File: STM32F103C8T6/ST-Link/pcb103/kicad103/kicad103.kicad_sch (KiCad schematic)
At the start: 31 parts, among them IC1 LD1117DT33TR, J1 0480372200, J2 Conn_01x02_Socket, J3 Conn_02x05_Odd_Even, J5 Conn_01x16_Pin, J7 Conn_01x04_Pin, J8 Conn_01x05_Socket, J9 Conn_01x17_Pin, U1 STM32F103C8T6, Y1 8MHz 20pF

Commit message: Generate BOM
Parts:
- C1: JLC # (none) -> C24497
- C2: JLC # (none) -> C15850
- C3, C4, C5, C6, C7: JLC # (none) -> C14663
- C8, C9: JLC # (none) -> C1557
- D1: JLC # (none) -> C8598
- D2: JLC # (none) -> C84256
- D3: JLC # (none) -> C2296
- IC1: JLC # (none) -> C132629
- J3: JLC # (none) -> C2881910
- R1, R2, R4, R5: JLC # (none) -> C4310
- R3: JLC # (none) -> C25118
- R6: JLC # (none) -> C2078575
- U1: JLC # (none) -> C8734
- Y1: JLC # (none) -> C115962
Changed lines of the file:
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@@
+      (effects (font (size 1.27 1.27)) hide)
+    )
+    (property "JLC #" "C25118" (at 45.085 100.33 0)
       (effects (font (size 1.27 1.27)) hide)
     )
@@
     )
     (property "Datasheet" "~" (at 198.12 146.685 0)
+      (effects (font (size 1.27 1.27)) hide)
+    )
+    (property "JLC #" "" (at 198.12 146.685 0)
       (effects (font (size 1.27 1.27)) hide)
     )
@@
       (effects (font (size 1.27 1.27)) hide)
     )
+    (property "JLC #" "C1557" (at 50.165 88.265 0)
+      (effects (font (size 1.27 1.27)) hide)
+    )
     (pin "1")
     (pin "2")
@@
       (effects (font (size 1.27 1.27)) (justify left top) hide)
     )
+    (property "JLC #" "C132629" (at 208.915 34.925 0)
+      (effects (font (size 1.27 1.27)) hide)
+    )
     (pin "1")
     (pin "3")
@@
       (effects (font (size 1.27 1.27)) hide)
     )
+    (property "JLC #" "C14663" (at 55.88 62.865 0)
+      (effects (font (size 1.27 1.27)) hide)
+    )
     (pin "1")
     (pin "2")
@@
     )
     (property "Datasheet" "~" (at 241.3 146.685 0)
+      (effects (font (size 1.27 1.27)) hide)
+    )
+    (property "JLC #" "" (at 241.3 146.685 0)
       (effects (font (size 1.27 1.27)) hide)
     )
@@
     )
     (property "Datasheet" "~" (at 95.25 62.865 0)
+      (effects (font (size 1.27 1.27)) hide)
+    )
+    (property "JLC #" "C14663" (at 95.25 62.865 0)
       (effects (font (size 1.27 1.27)) hide)
     )
@@
       (effects (font (size 1.27 1.27)) hide)
     )
+    (property "JLC #" "C1557" (at 37.465 105.41 0)
+      (effects (font (size 1.27 1.27)) hide)
+    )
     (pin "1")
     (pin "2")
@@
       (effects (font (size 1.27 1.27)) hide)
     )
+    (property "JLC #" "" (at 163.83 38.735 0)
+      (effects (font (size 1.27 1.27)) hide)
+    )
     (pin "1")
     (pin "2")
@@
     )
     (property "Datasheet" "~" (at 15.24 29.845 0)
+      (effects (font (size 1.27 1.27)) hide)
+    )
+    (property "JLC #" "" (at 15.24 29.845 0)
       (effects (font (size 1.27 1.27)) hide)
     )
@@
     )
     (property "Datasheet" "~" (at 199.39 104.14 0)
+      (effects (font (size 1.27 1.27)) hide)
+    )
+    (property "JLC #" "" (at 199.39 104.14 0)
       (effects (font (size 1.27 1.27)) hide)
     )
@@
       (effects (font (size 1.27 1.27)) hide)
     )
+    (property "JLC #" "C4310" (at 274.32 42.545 0)
+      (effects (font (size 1.27 1.27)) hide)
+    )
     (pin "1")
     (pin "2")
@@
       (effects (font (size 1.27 1.27)) hide)
     )
+    (property "JLC #" "C14663" (at 69.215 62.865 0)
+      (effects (font (size 1.27 1.27)) hide)
+    )
     (pin "1")
     (pin "2")
@@
     )
     (property "Datasheet" "~" (at 15.24 22.86 0)
+      (effects (font (size 1.27 1.27)) hide)
+    )
+    (property "JLC #" "" (at 15.24 22.86 0)
       (effects (font (size 1.27 1.27)) hide)
     )
@@
     )
     (property "Datasheet" "~" (at 39.37 173.355 0)
+      (effects (font (size 1.27 1.27)) hide)
+    )
+    (property "JLC #" "C2881910" (at 39.37 173.355 0)
       (effects (font (size 1.27 1.27)) hide)
     )
@@
       (effects (font (size 1.27 1.27)) hide)
     )
+    (property "JLC #" "C15850" (at 252.095 41.275 0)
+      (effects (font (size 1.27 1.27)) hide)
+    )
     (pin "1")
     (pin "2")
@@
       (effects (font (size 1.27 1.27)) hide)
     )
+    (property "JLC #" "C24497" (at 196.85 35.56 0)
+      (effects (font (size 1.27 1.27)) hide)
+    )
     (pin "1")
     (pin "2")
@@
     )
     (property "Datasheet" "~" (at 131.445 110.49 0)
+      (effects (font (size 1.27 1.27)) hide)
+    )
+    (property "JLC #" "C4310" (at 131.445 110.49 0)
       (effects (font (size 1.27 1.27)) hide)
     )
@@
       (effects (font (size 1.27 1.27)) hide)
     )
+    (property "JLC #" "C2296" (at 52.07 107.95 0)
+      (effects (font (size 1.27 1.27)) hide)
+    )
     (pin "1")
     (pin "2")
@@
     )
     (property "Datasheet" "~" (at 266.065 34.925 0)
+      (effects (font (size 1.27 1.27)) hide)
+    )
+    (property "JLC #" "C84256" (at 266.065 34.925 0)
       (effects (font (size 1.27 1.27)) hide)
     )
@@
       (effects (font (size 1.27 1.27)) hide)
     )
+    (property "JLC #" "C115962" (at 37.465 89.535 0)
+      (effects (font (size 1.27 1.27)) hide)
+    )
     (pin "1")
     (pin "2")
@@
     )
     (property "Datasheet" "https://www.st.com/resource/en/datasheet/stm32f103c8.pdf" (at 84.455 125.73 0)
+      (effects (font (size 1.27 1.27)) hide)
+    )
+    (property "JLC #" "C8734" (at 84.455 125.73 0)
       (effects (font (size 1.27 1.27)) hide)
     )
@@
       (effects (font (size 1.27 1.27)) hide)
     )
+    (property "JLC #" "" (at 15.24 15.875 0)
+      (effects (font (size 1.27 1.27)) hide)
+    )
     (pin "1")
     (instances
@@
     (property "Arrow Price/Stock" "https://www.arrow.com/en/products/0480372200/molex?region=nac" (at 129.54 -958.725 0)
       (effects (font (size 1.27 1.27)) (justify left top) hide)
+    )
+    (property "JLC #" "" (at 113.03 36.195 0)
+      (effects (font (size 1.27 1.27)) hide)
     )
     (pin "1")
@@
       (effects (font (size 1.27 1.27)) hide)
     )
+    (property "JLC #" "C4310" (at 50.165 133.35 0)
+      (effects (font (size 1.27 1.27)) hide)
+    )
     (pin "1")
     (pin "2")
@@
       (effects (font (size 1.27 1.27)) hide)
     )
+    (property "JLC #" "C4310" (at 43.18 115.57 0)
+      (effects (font (size 1.27 1.27)) hide)
+    )
     (pin "1")
     (pin "2")
@@
     )
     (property "Datasheet" "~" (at 238.76 104.14 0)
+      (effects (font (size 1.27 1.27)) hide)
+    )
+    (property "JLC #" "" (at 238.76 104.14 0)
       (effects (font (size 1.27 1.27)) hide)
     )
@@
       (effects (font (size 1.27 1.27)) hide)
     )
+    (property "JLC #" "C8598" (at 186.69 28.575 0)
+      (effects (font (size 1.27 1.27)) hide)
+    )
     (pin "1")
     (pin "2")
@@
       (effects (font (size 1.27 1.27)) hide)
     )
+    (property "JLC #" "C14663" (at 82.55 62.865 0)
+      (effects (font (size 1.27 1.27)) hide)
+    )
     (pin "1")
     (pin "2")
@@
       (effects (font (size 1.27 1.27)) hide)
     )
+    (property "JLC #" "C2078575" (at 137.16 150.495 0)
+      (effects (font (size 1.27 1.27)) hide)
+    )
     (pin "1")
     (pin "2")
@@
       (effects (font (size 1.27 1.27)) hide)
     )
+    (property "JLC #" "C14663" (at 107.95 62.865 0)
+      (effects (font (size 1.27 1.27)) hide)
+    )

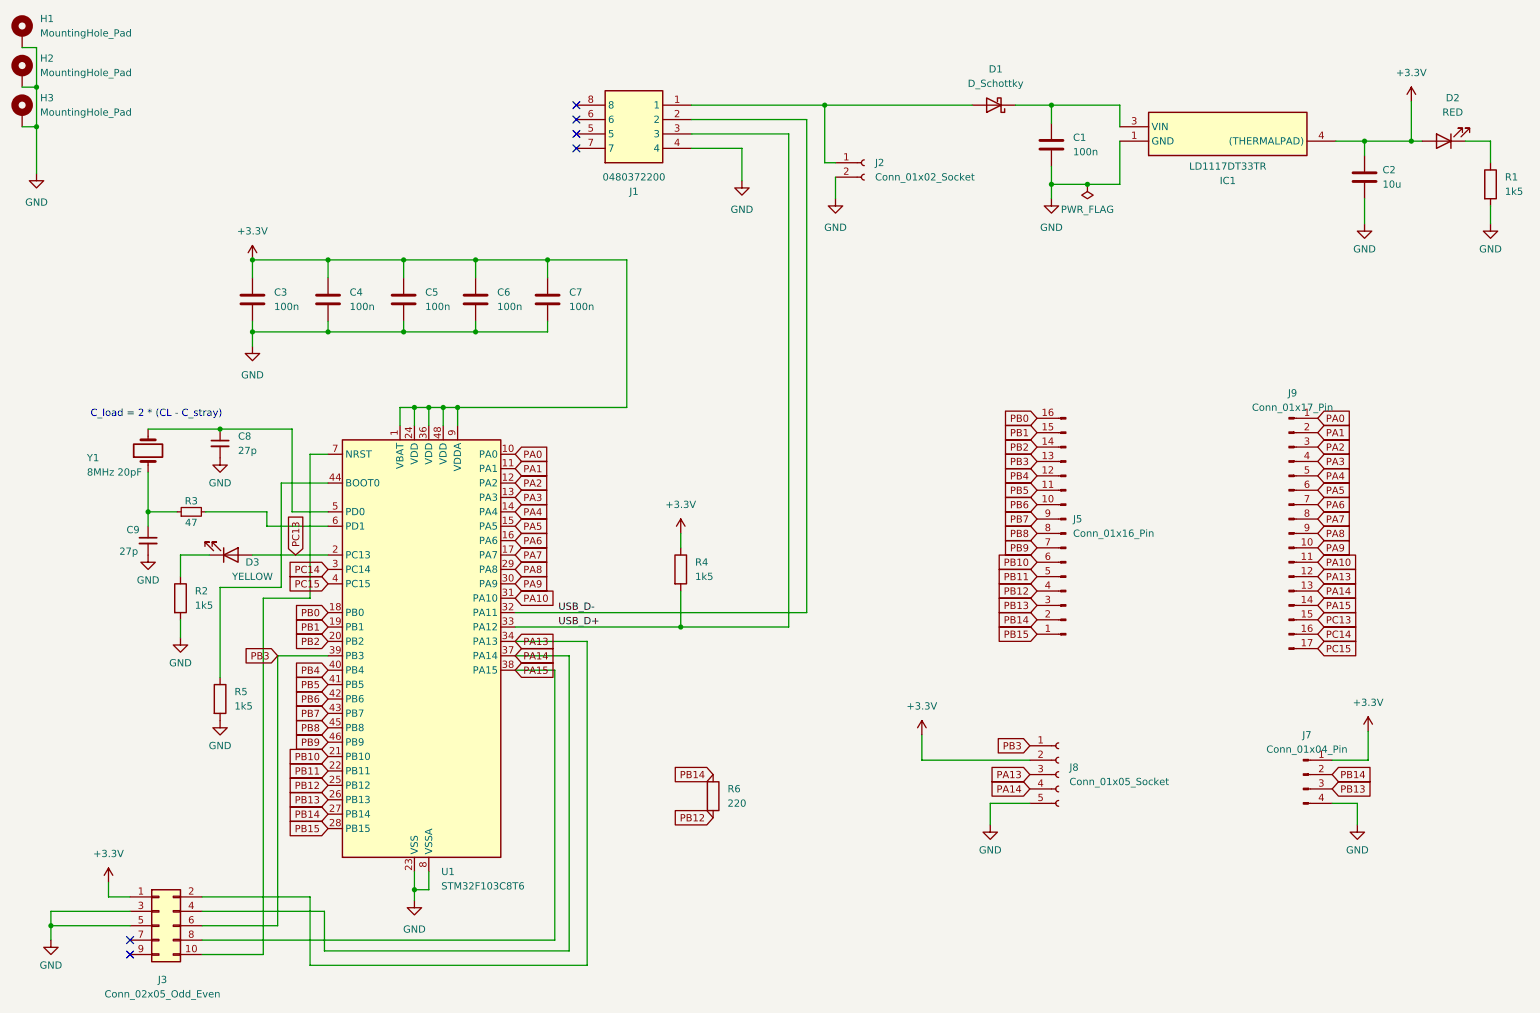
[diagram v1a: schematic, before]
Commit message: Replace 3.3V regulator
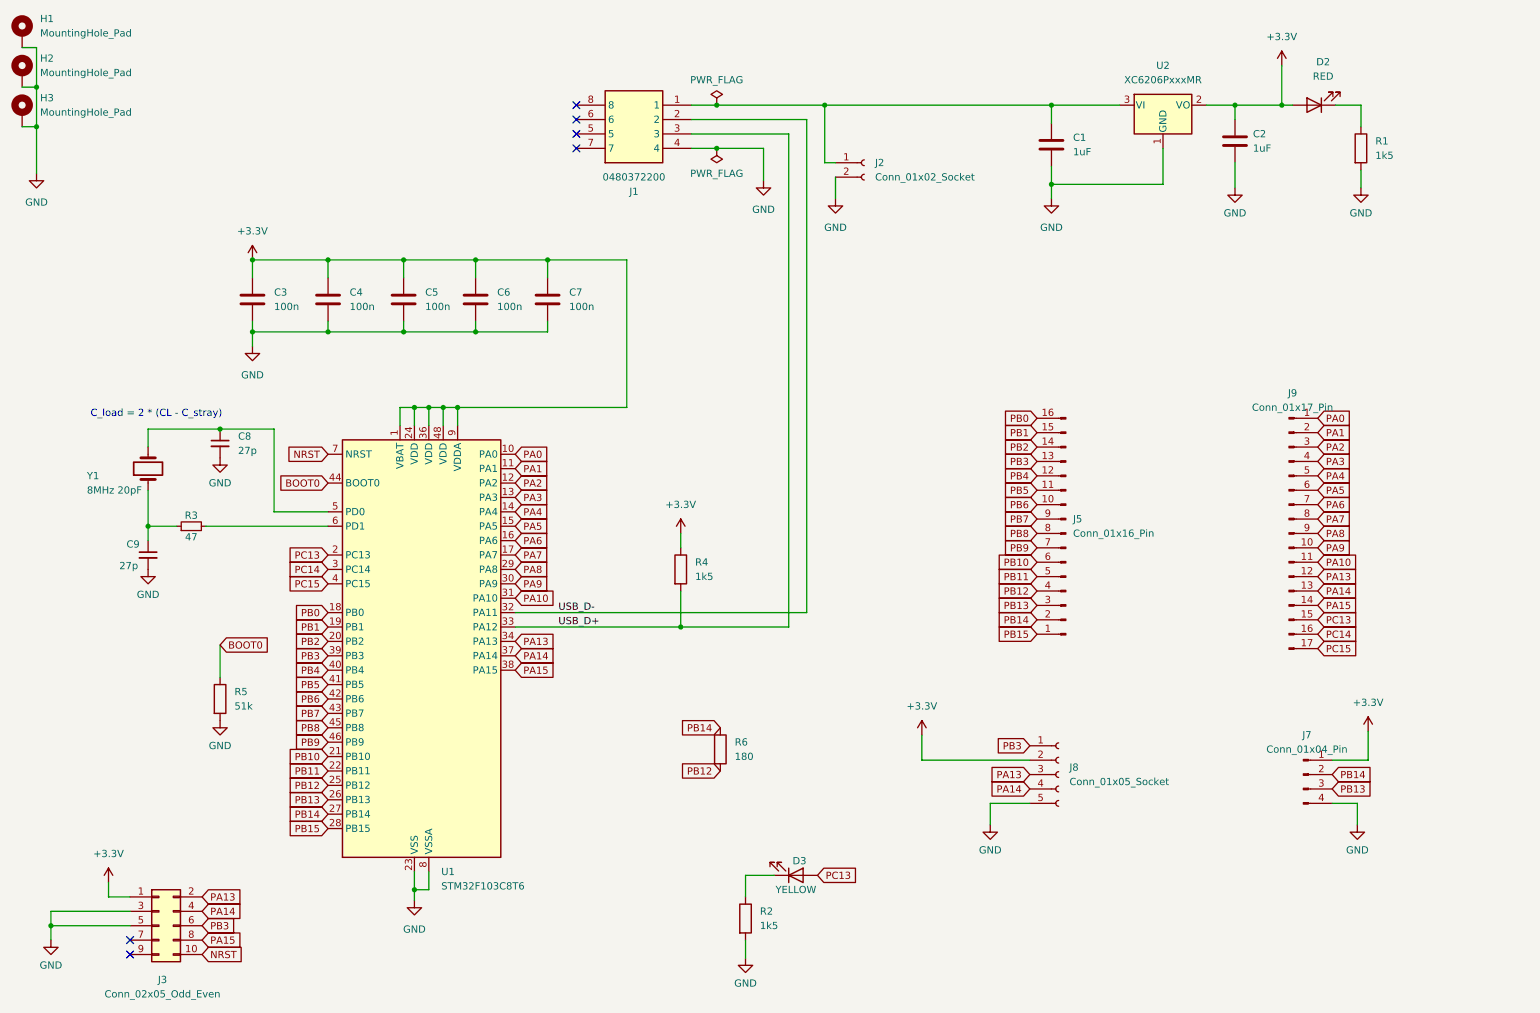
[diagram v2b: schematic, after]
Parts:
- removed D1: D_Schottky, Diode_SMD:D_SOD-123, symbol Device:D_Schottky
- removed IC1: LD1117DT33TR, Library:TO228P972X240-3N, symbol New_Library:LD1117DT33TR
- added U2: XC6206PxxxMR, Package_TO_SOT_SMD:SOT-23-3, symbol Regulator_Linear:XC6206PxxxMR
- C1: value 100n -> 1uF; footprint Capacitor_SMD:C_1206_3216Metric -> Capacitor_SMD:C_0805_2012Metric; JLC # C24497 -> C28323
- C2: value 10u -> 1uF; JLC # C15850 -> C28323
- R5: value 1k5 -> 51k; JLC # C4310 -> C17737
- R6: value 220 -> 180; JLC # C2078575 -> C17924
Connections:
- net +3.3V: now also U2.2 (VO)
- net GND: now also U2.1 (GND)
- net at C1.1: now also J1.1, J2.1 (Pin_1), U2.3 (VI)
- net NRST: now reaches J3.10 (Pin_10), U1.7 (NRST)
- net BOOT0: now reaches R5.1, U1.44 (BOOT0)
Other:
- moved on the sheet: C2, C9, D2, D3, R1, R2, R3, R6, Y1
